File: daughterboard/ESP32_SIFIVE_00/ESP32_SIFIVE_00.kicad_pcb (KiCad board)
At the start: 4 copper layers, 67 x 50 mm, 2 parts, among them J1 m2_keyA_67pin_daughterboard

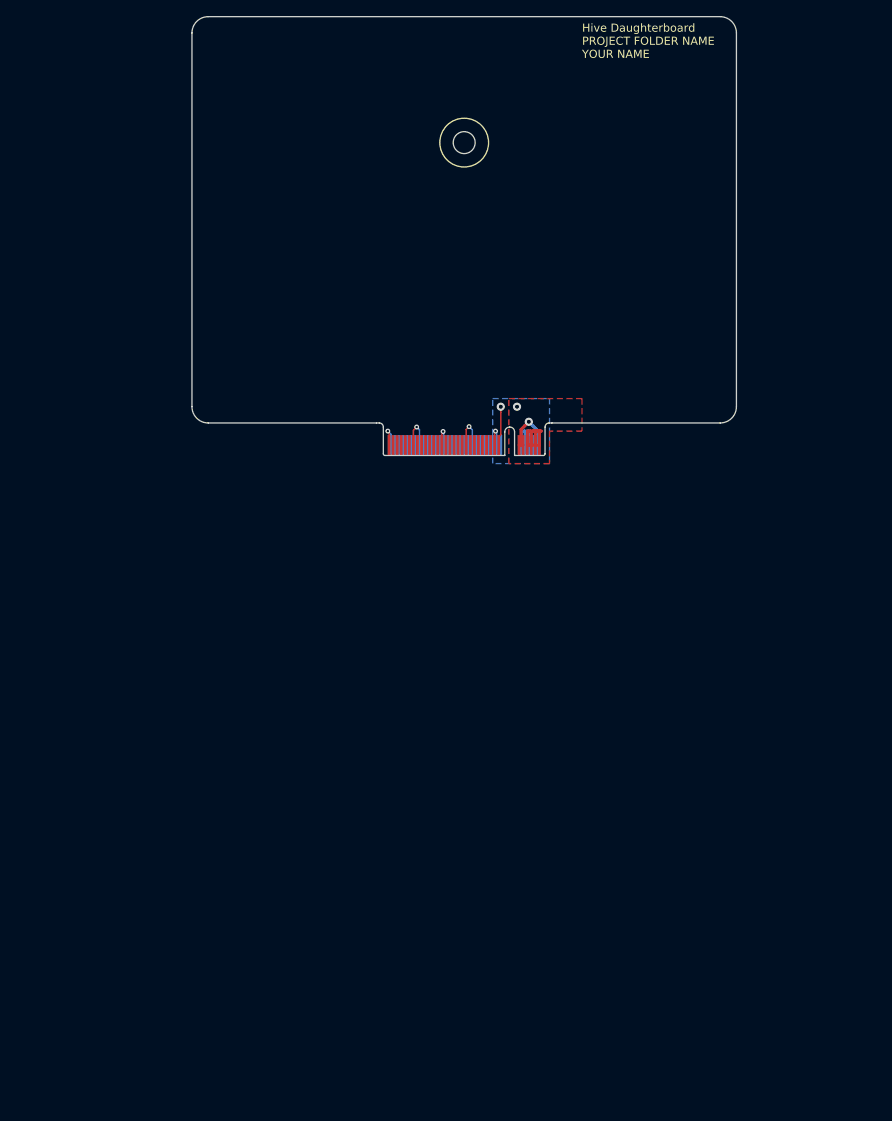
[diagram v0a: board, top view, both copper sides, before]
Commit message: started with esp32/sifive layout
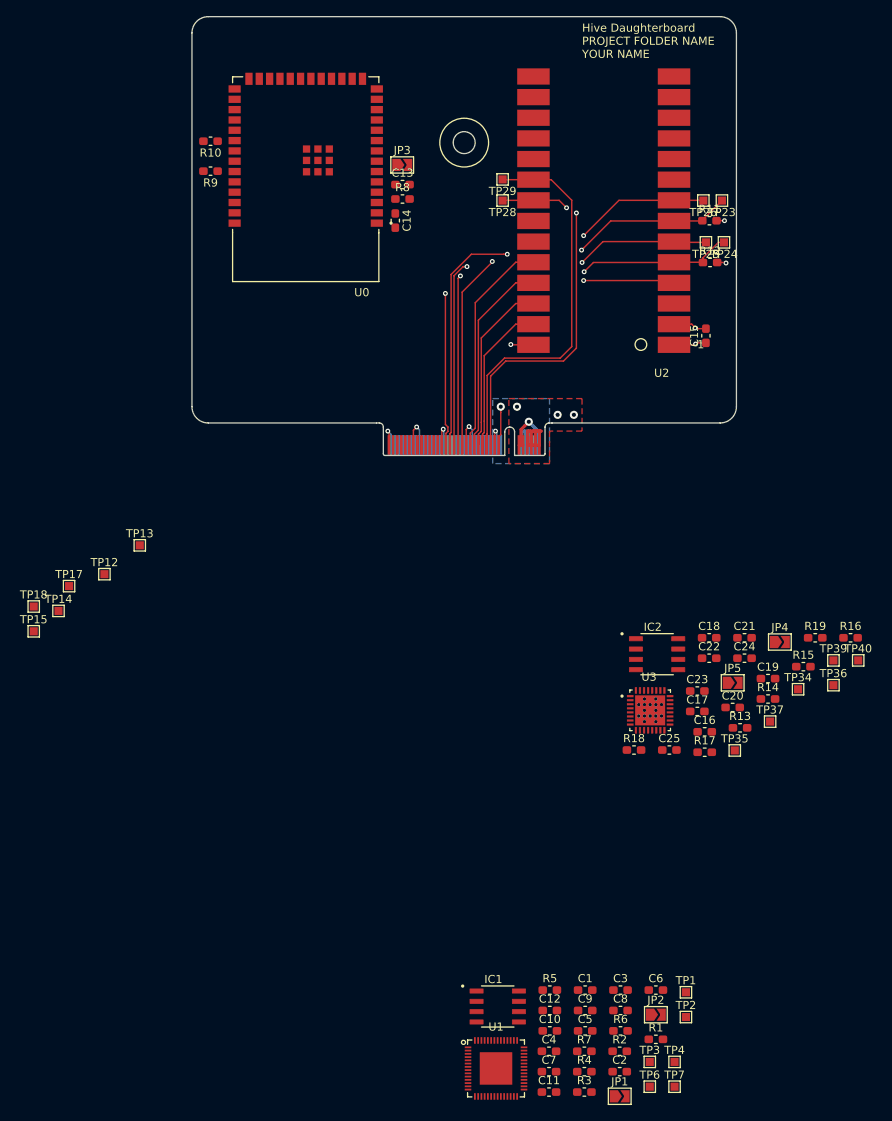
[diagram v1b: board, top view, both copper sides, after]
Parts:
- added C1: 100n, Capacitor_SMD:C_0603_1608Metric_Pad1.05x0.95mm_HandSolder, F.Cu at (163.4, 196.8)
- added C10: 100n, Capacitor_SMD:C_0603_1608Metric_Pad1.05x0.95mm_HandSolder, F.Cu at (159.0, 201.8)
- added C11: 100n, Capacitor_SMD:C_0603_1608Metric_Pad1.05x0.95mm_HandSolder, F.Cu at (158.9, 209.3)
- added C12: 100n, Capacitor_SMD:C_0603_1608Metric_Pad1.05x0.95mm_HandSolder, F.Cu at (159.0, 199.3)
- added C13: 100n, Capacitor_SMD:C_0603_1608Metric_Pad1.05x0.95mm_HandSolder, F.Cu at (140.9, 97.7)
- added C14: 10u, Capacitor_SMD:C_0603_1608Metric_Pad1.05x0.95mm_HandSolder, F.Cu at (140.0, 102.1)
- added C15: 10u, Capacitor_SMD:C_0603_1608Metric_Pad1.05x0.95mm_HandSolder, F.Cu at (178.2, 116.3)
- added C16: 100n, Capacitor_SMD:C_0603_1608Metric_Pad1.05x0.95mm_HandSolder, F.Cu at (178.1, 165.0)
- added C17: 1u, Capacitor_SMD:C_0603_1608Metric_Pad1.05x0.95mm_HandSolder, F.Cu at (177.2, 162.5)
- added C18: 100n, Capacitor_SMD:C_0603_1608Metric_Pad1.05x0.95mm_HandSolder, F.Cu at (178.6, 153.4)
- added C19: 10u, Capacitor_SMD:C_0603_1608Metric_Pad1.05x0.95mm_HandSolder, F.Cu at (185.9, 158.5)
- added C2: 1u, Capacitor_SMD:C_0603_1608Metric_Pad1.05x0.95mm_HandSolder, F.Cu at (167.6, 206.8)
- added C20: 1u, Capacitor_SMD:C_0603_1608Metric_Pad1.05x0.95mm_HandSolder, F.Cu at (181.5, 162.0)
- added C21: 100n, Capacitor_SMD:C_0603_1608Metric_Pad1.05x0.95mm_HandSolder, F.Cu at (183.0, 153.4)
- added C22: 100n, Capacitor_SMD:C_0603_1608Metric_Pad1.05x0.95mm_HandSolder, F.Cu at (178.6, 155.9)
- added C23: 100n, Capacitor_SMD:C_0603_1608Metric_Pad1.05x0.95mm_HandSolder, F.Cu at (177.2, 160.0)
- added C24: 100n, Capacitor_SMD:C_0603_1608Metric_Pad1.05x0.95mm_HandSolder, F.Cu at (183.0, 155.9)
- added C25: 100n, Capacitor_SMD:C_0603_1608Metric_Pad1.05x0.95mm_HandSolder, F.Cu at (173.7, 167.2)
- added C3: 100n, Capacitor_SMD:C_0603_1608Metric_Pad1.05x0.95mm_HandSolder, F.Cu at (167.7, 196.8)
- added C4: 10u, Capacitor_SMD:C_0603_1608Metric_Pad1.05x0.95mm_HandSolder, F.Cu at (158.9, 204.3)
- added C5: 1u, Capacitor_SMD:C_0603_1608Metric_Pad1.05x0.95mm_HandSolder, F.Cu at (163.4, 201.8)
- added C6: 100n, Capacitor_SMD:C_0603_1608Metric_Pad1.05x0.95mm_HandSolder, F.Cu at (172.1, 196.8)
- added C7: 100n, Capacitor_SMD:C_0603_1608Metric_Pad1.05x0.95mm_HandSolder, F.Cu at (158.9, 206.8)
- added C8: 100n, Capacitor_SMD:C_0603_1608Metric_Pad1.05x0.95mm_HandSolder, F.Cu at (167.7, 199.3)
- added C9: 100n, Capacitor_SMD:C_0603_1608Metric_Pad1.05x0.95mm_HandSolder, F.Cu at (163.4, 199.3)
- added IC1: W25X40CLSNIG, hive_daughterboard:W25X40CLSNIG, F.Cu at (152.6, 198.8)
- added IC2: W25X40CLSNIG, hive_daughterboard:W25X40CLSNIG, F.Cu at (172.2, 155.5)
- added JP1: BOOT, Jumper:SolderJumper-2_P1.3mm_Open_TrianglePad1.0x1.5mm, F.Cu at (167.6, 209.9)
- added JP2: NRST, Jumper:SolderJumper-2_P1.3mm_Open_TrianglePad1.0x1.5mm, F.Cu at (172.1, 199.8)
- added JP3: NRST, Jumper:SolderJumper-2_P1.3mm_Open_TrianglePad1.0x1.5mm, F.Cu at (140.9, 95.2)
- added JP4: NRST, Jumper:SolderJumper-2_P1.3mm_Open_TrianglePad1.0x1.5mm, F.Cu at (187.3, 154.0)
- added JP5: BOOT, Jumper:SolderJumper-2_P1.3mm_Open_TrianglePad1.0x1.5mm, F.Cu at (181.5, 159.0)
- added R1: 100k, Resistor_SMD:R_0603_1608Metric_Pad1.05x0.95mm_HandSolder, F.Cu at (172.1, 202.8)
- added R10: 10k, Resistor_SMD:R_0603_1608Metric_Pad1.05x0.95mm_HandSolder, F.Cu at (117.3, 92.3)
- added R11: 10k, Resistor_SMD:R_0603_1608Metric_Pad1.05x0.95mm_HandSolder, F.Cu at (178.7, 102.1)
- added R12: 10k, Resistor_SMD:R_0603_1608Metric_Pad1.05x0.95mm_HandSolder, F.Cu at (178.8, 107.3)
- added R13: 100k, Resistor_SMD:R_0603_1608Metric_Pad1.05x0.95mm_HandSolder, F.Cu at (182.4, 164.5)
- added R14: 10k, Resistor_SMD:R_0603_1608Metric_Pad1.05x0.95mm_HandSolder, F.Cu at (185.9, 161.0)
- added R15: 10k, Resistor_SMD:R_0603_1608Metric_Pad1.05x0.95mm_HandSolder, F.Cu at (190.2, 157.0)
- added R16: 10k, Resistor_SMD:R_0603_1608Metric_Pad1.05x0.95mm_HandSolder, F.Cu at (196.0, 153.4)
- added R17: 100k, Resistor_SMD:R_0603_1608Metric_Pad1.05x0.95mm_HandSolder, F.Cu at (178.1, 167.5)
- added R18: 100k, Resistor_SMD:R_0603_1608Metric_Pad1.05x0.95mm_HandSolder, F.Cu at (169.4, 167.2)
- added R19: 100k, Resistor_SMD:R_0603_1608Metric_Pad1.05x0.95mm_HandSolder, F.Cu at (191.7, 153.4)
- added R2: 10k, Resistor_SMD:R_0603_1608Metric_Pad1.05x0.95mm_HandSolder, F.Cu at (167.6, 204.3)
- added R3: 10k, Resistor_SMD:R_0603_1608Metric_Pad1.05x0.95mm_HandSolder, F.Cu at (163.3, 209.3)
- added R4: 10k, Resistor_SMD:R_0603_1608Metric_Pad1.05x0.95mm_HandSolder, F.Cu at (163.3, 206.8)
- added R5: 100k, Resistor_SMD:R_0603_1608Metric_Pad1.05x0.95mm_HandSolder, F.Cu at (159.0, 196.8)
- added R6: 100k, Resistor_SMD:R_0603_1608Metric_Pad1.05x0.95mm_HandSolder, F.Cu at (167.7, 201.8)
- added R7: 100k, Resistor_SMD:R_0603_1608Metric_Pad1.05x0.95mm_HandSolder, F.Cu at (163.3, 204.3)
- added R8: 100k, Resistor_SMD:R_0603_1608Metric_Pad1.05x0.95mm_HandSolder, F.Cu at (140.9, 99.4)
- added R9: 10k, Resistor_SMD:R_0603_1608Metric_Pad1.05x0.95mm_HandSolder, F.Cu at (117.3, 96.0)
- added TP1: TMS, TestPoint:TestPoint_Pad_1.0x1.0mm, F.Cu at (175.8, 197.1)
- added TP12: TMS, TestPoint:TestPoint_Pad_1.0x1.0mm, F.Cu at (104.2, 145.6)
- added TP13: TCK, TestPoint:TestPoint_Pad_1.0x1.0mm, F.Cu at (108.6, 142.1)
- added TP14: TDO, TestPoint:TestPoint_Pad_1.0x1.0mm, F.Cu at (98.6, 150.1)
- added TP15: TDI, TestPoint:TestPoint_Pad_1.0x1.0mm, F.Cu at (95.5, 152.6)
- added TP17: UART_TX, TestPoint:TestPoint_Pad_1.0x1.0mm, F.Cu at (99.9, 147.1)
- added TP18: UART_RX, TestPoint:TestPoint_Pad_1.0x1.0mm, F.Cu at (95.5, 149.6)
- added TP2: TCK, TestPoint:TestPoint_Pad_1.0x1.0mm, F.Cu at (175.8, 200.1)
- added TP23: TMS, TestPoint:TestPoint_Pad_1.0x1.0mm, F.Cu at (180.2, 99.6)
- added TP24: TCK, TestPoint:TestPoint_Pad_1.0x1.0mm, F.Cu at (180.5, 104.8)
- added TP25: TDO, TestPoint:TestPoint_Pad_1.0x1.0mm, F.Cu at (178.2, 104.8)
- added TP26: TDI, TestPoint:TestPoint_Pad_1.0x1.0mm, F.Cu at (177.9, 99.6)
- added TP28: UART_TX, TestPoint:TestPoint_Pad_1.0x1.0mm, F.Cu at (153.2, 99.6)
- added TP29: UART_RX, TestPoint:TestPoint_Pad_1.0x1.0mm, F.Cu at (153.2, 97.0)
- added TP3: TDO, TestPoint:TestPoint_Pad_1.0x1.0mm, F.Cu at (171.3, 205.6)
- added TP34: TMS, TestPoint:TestPoint_Pad_1.0x1.0mm, F.Cu at (189.6, 159.8)
- added TP35: TCK, TestPoint:TestPoint_Pad_1.0x1.0mm, F.Cu at (181.8, 167.3)
- added TP36: TDO, TestPoint:TestPoint_Pad_1.0x1.0mm, F.Cu at (193.9, 159.3)
- added TP37: TDI, TestPoint:TestPoint_Pad_1.0x1.0mm, F.Cu at (186.1, 163.7)
- added TP39: UART_TX, TestPoint:TestPoint_Pad_1.0x1.0mm, F.Cu at (193.9, 156.2)
- added TP4: TDI, TestPoint:TestPoint_Pad_1.0x1.0mm, F.Cu at (174.4, 205.6)
- added TP40: UART_RX, TestPoint:TestPoint_Pad_1.0x1.0mm, F.Cu at (197.0, 156.2)
- added TP6: UART_TX, TestPoint:TestPoint_Pad_1.0x1.0mm, F.Cu at (171.3, 208.7)
- added TP7: UART_RX, TestPoint:TestPoint_Pad_1.0x1.0mm, F.Cu at (174.4, 208.7)
- added U0: ESP32-S3-WROOM-1-N8R8, hive_daughterboard:XCVR_ESP32-S3-WROOM-1-N8R8, F.Cu at (129.0, 94.0)
- added U1: ESP32-S2, hive_daughterboard:ESP32-S2, F.Cu at (152.4, 206.4)
- added U2: LoFive-R1, hive_daughterboard:LoFive-R1, F.Cu at (165.7, 118.9)
- added U3: ESP32-C3, hive_daughterboard:ESP32-C3, F.Cu at (171.4, 162.4)
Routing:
- net /Target 2/TDI|NC_2: track 0.00 -> 55.9 mm, vias 0 -> 2
- net /Target 2/TMS|SWDIO_2: track 0.00 -> 55.6 mm, vias 0 -> 2
- net /Target 2/TCK|SWDCLK_2: track 0.00 -> 55.5 mm, vias 0 -> 2
- net /Target 2/TDO|SWO_2: track 0.00 -> 53.6 mm, vias 0 -> 2
- net /Target 2/UART_TxD2: track 0.00 -> 48.1 mm
- net /Target 2/RST_2: track 0.00 -> 47.8 mm, vias 0 -> 2
- net /Target 2/UART_RxD2: track 0.00 -> 46.9 mm, vias 0 -> 2
- net /Target 2/GPIO2.0: track 0.00 -> 27.0 mm
- net /Target 2/GPIO2.1: track 0.00 -> 24.3 mm
- net /Target 2/GPIO2.2: track 0.00 -> 21.5 mm
- net /Target 2/GPIO2.3: track 0.00 -> 18.8 mm
- net GND: track 28.1 -> 36.8 mm, vias 6 -> 9
- net +5V: track 11.6 -> 15.6 mm, vias 0 -> 3
- net +3V3: track 11.6 -> 12.5 mm, vias 2 -> 3
- added copper zone on PWR_SIG.Cu, net +5V

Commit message: finished ESP32_SIFIVE daughterboard layout
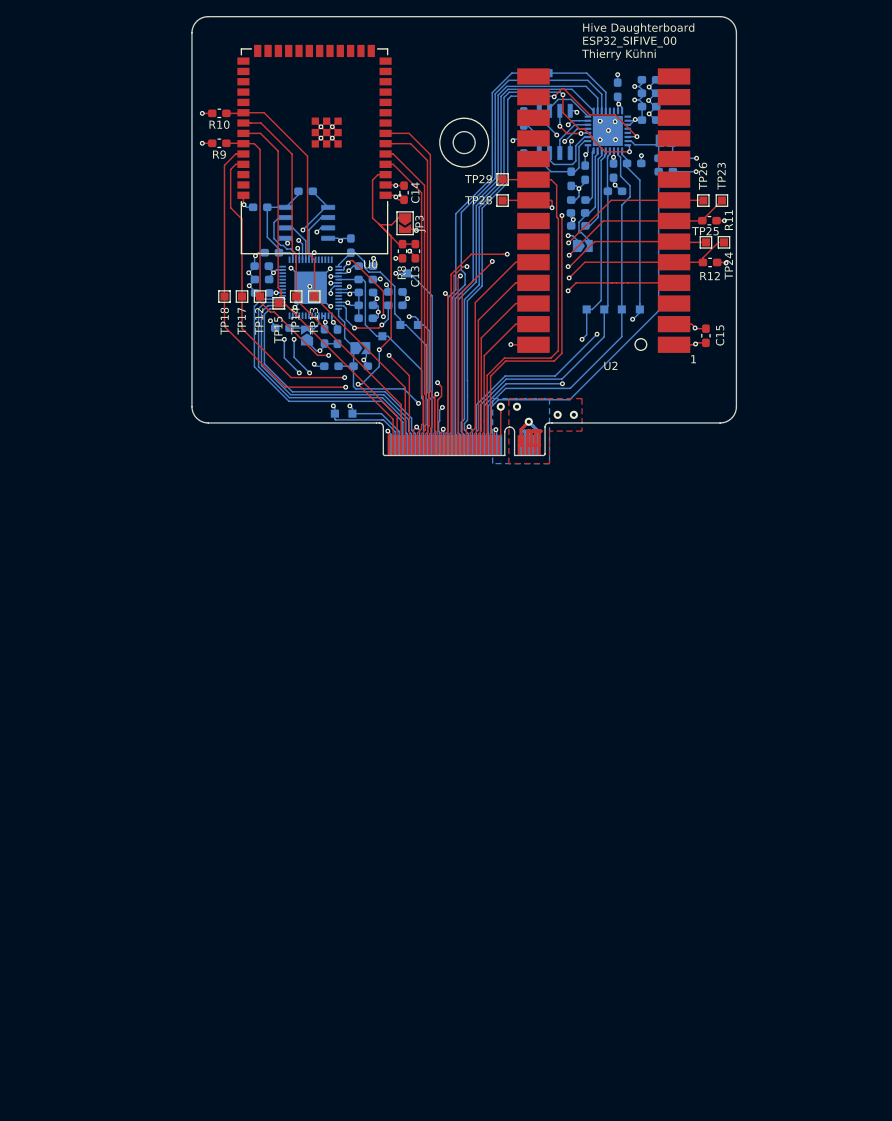
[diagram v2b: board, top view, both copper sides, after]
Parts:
- C1, C10, C11, C12, C16, C17, C18, C19, C2, C20, C21, C22, C23, C24, C25, C3, C4, C5, C6, C7, C8, C9, IC1, IC2, JP1, JP2, JP4, JP5, R1, R13, R14, R15, R16, R17, R18, R19, R2, R3, R4, R5, R6, R7, TP1, TP2, TP3, TP34, TP35, TP36, TP37, TP39, TP4, TP40, TP6, TP7, U1: moved to B.Cu
- U3: value ESP32-C3 -> QFN50P500X500X90-33N; moved to B.Cu
- moved R4 113.6 mm to (129.0, 98.5), turned to 180 degrees
- moved C2 109.5 mm to (124.8, 106.0), turned to 180 degrees
- moved R3 108.1 mm to (134.6, 105.2), turned to 90 degrees
- moved C11 107.6 mm to (123.6, 107.7), turned to 180 degrees
- moved C3 106.0 mm to (123.4, 100.5), turned to 180 degrees
- moved TP4 102.5 mm to (141.5, 108.6)
- moved C4 101.3 mm to (123.6, 109.3), turned to 180 degrees
- moved JP1 101.2 mm to (129.2, 116.2), turned to 90 degrees
- moved R2 100.0 mm to (136.4, 109.3)
- moved IC1 99.3 mm to (129.2, 102.4), turned to 180 degrees
- moved U1 98.7 mm to (129.6, 110.4), turned to 90 degrees
- moved C5 97.9 mm to (136.4, 107.7)
- moved C10 97.5 mm to (123.6, 111.0), turned to 180 degrees
- moved R7 96.3 mm to (140.0, 110.9), turned to 180 degrees
- moved TP3 95.1 mm to (142.8, 114.9)
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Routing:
- net GND: track 36.8 -> 125.4 mm, vias 9 -> 48
- net /Target 3/GPIO3.1: track 0.00 -> 66.2 mm, vias 0 -> 2
- net /Target 3/GPIO3.0: track 0.00 -> 65.2 mm, vias 0 -> 2
- net /Target 3/UART_RxD3: track 0.00 -> 64.3 mm
- net /Target 3/UART_TxD3: track 0.00 -> 62.4 mm
- net /Target 3/GPIO3.3: track 0.00 -> 60.2 mm
- net /Target 0/UART_TxD0: track 0.00 -> 58.8 mm, vias 0 -> 2
- net /Target 3/GPIO3.2: track 0.00 -> 58.1 mm
- net /Target 0/UART_RxD0: track 0.00 -> 56.9 mm, vias 0 -> 2
- net /Target 3/RST_3: track 0.00 -> 55.6 mm
- net /Target 0/TMS|SWDIO_0: track 0.00 -> 54.0 mm, vias 0 -> 2
- net /Target 0/TCK|SWDCLK_0: track 0.00 -> 52.8 mm
- net +3V3: track 12.5 -> 64.2 mm, vias 3 -> 25
- net /Target 3/TMS|SWDIO_3: track 0.00 -> 50.7 mm, vias 0 -> 2
- net /Target 0/TDO|SWO_0: track 0.00 -> 49.0 mm
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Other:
- board text added: "Hive Daughterboard ESP32_SIFIVE_00 Thierry Kühni"
- board text removed: "Hive Daughterboard PROJECT FOLDER NAME YOUR NAME"

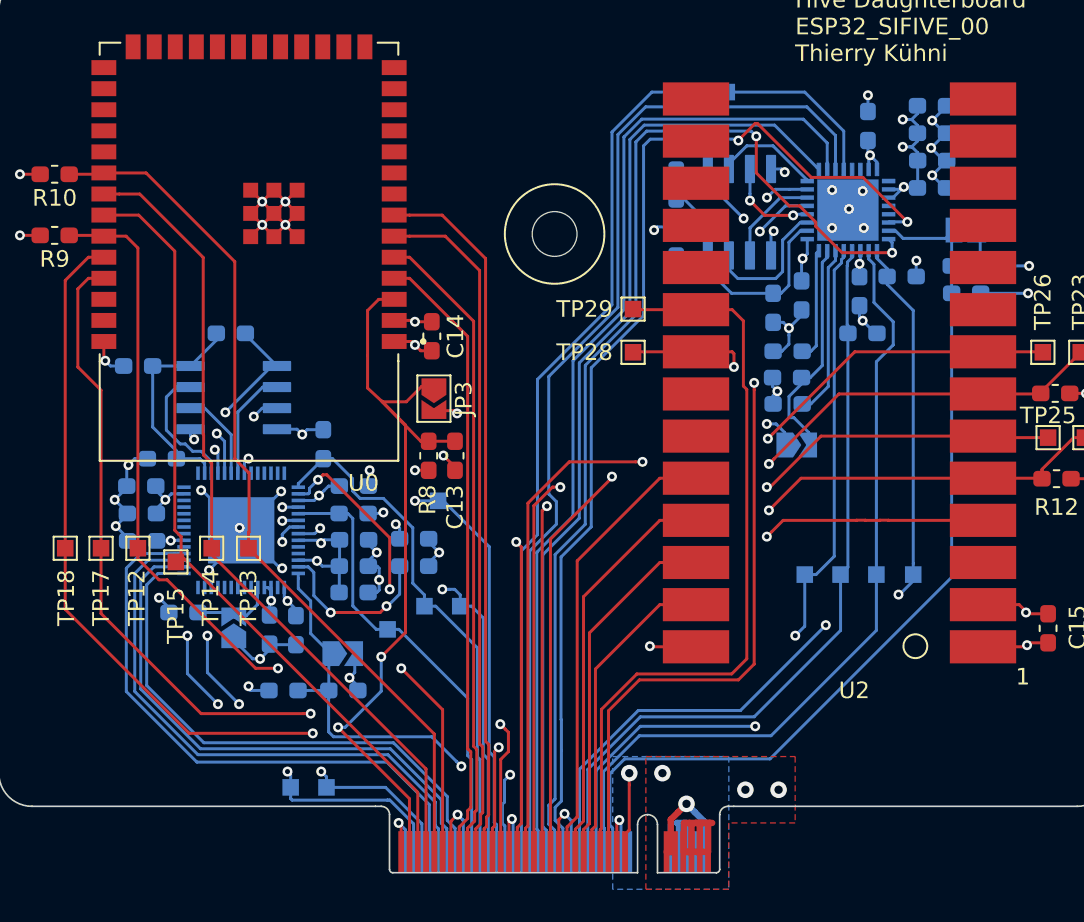
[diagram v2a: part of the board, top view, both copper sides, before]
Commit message: length matching daughterboards
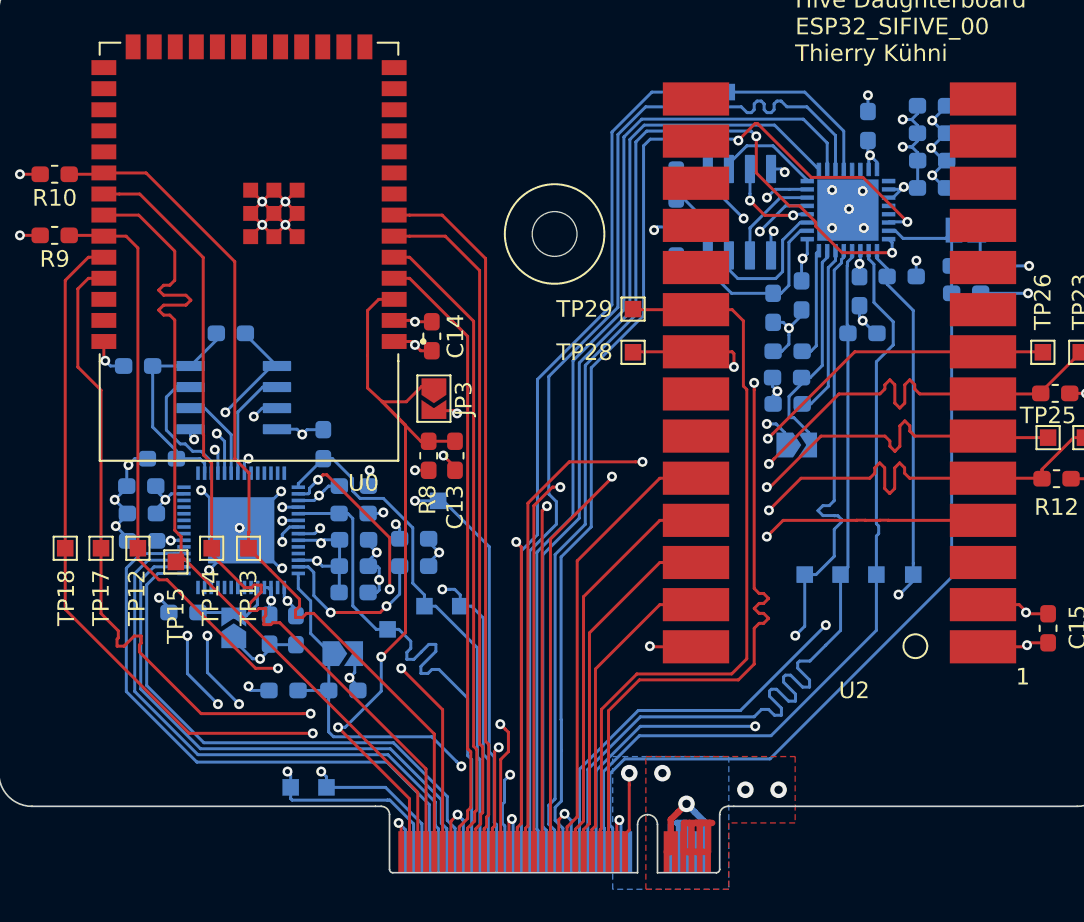
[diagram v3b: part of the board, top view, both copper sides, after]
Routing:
- net /Target 3/TCK|SWDCLK_3: track 46.9 -> 54.0 mm
- net /Target 0/TDI|NC_0: track 47.5 -> 51.9 mm
- net /Target 1/TMS|SWDIO_1: track 27.3 -> 31.5 mm
- net /Target 2/TCK|SWDCLK_2: track 55.7 -> 59.8 mm
- net /Target 2/TMS|SWDIO_2: track 55.6 -> 59.3 mm
- net /Target 0/TDO|SWO_0: track 49.0 -> 51.9 mm
- net /Target 2/TDO|SWO_2: track 53.6 -> 56.3 mm
- net /Target 1/UART_TxD1: track 30.1 -> 32.6 mm
- net /Target 2/UART_RxD2: track 44.0 -> 46.0 mm
- net /Target 3/TDO|SWO_3: track 47.0 -> 48.9 mm
- net /Target 0/UART_RxD0: track 56.9 -> 58.8 mm
- net /Target 3/UART_TxD3: track 62.4 -> 64.2 mm
- net /Target 0/TCK|SWDCLK_0: track 52.8 -> 54.0 mm
